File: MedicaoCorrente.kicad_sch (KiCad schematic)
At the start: 11 parts, among them J1 Conn_01x02, J2 Conn_01x02, J3 Conn_01x02, U4 LM324

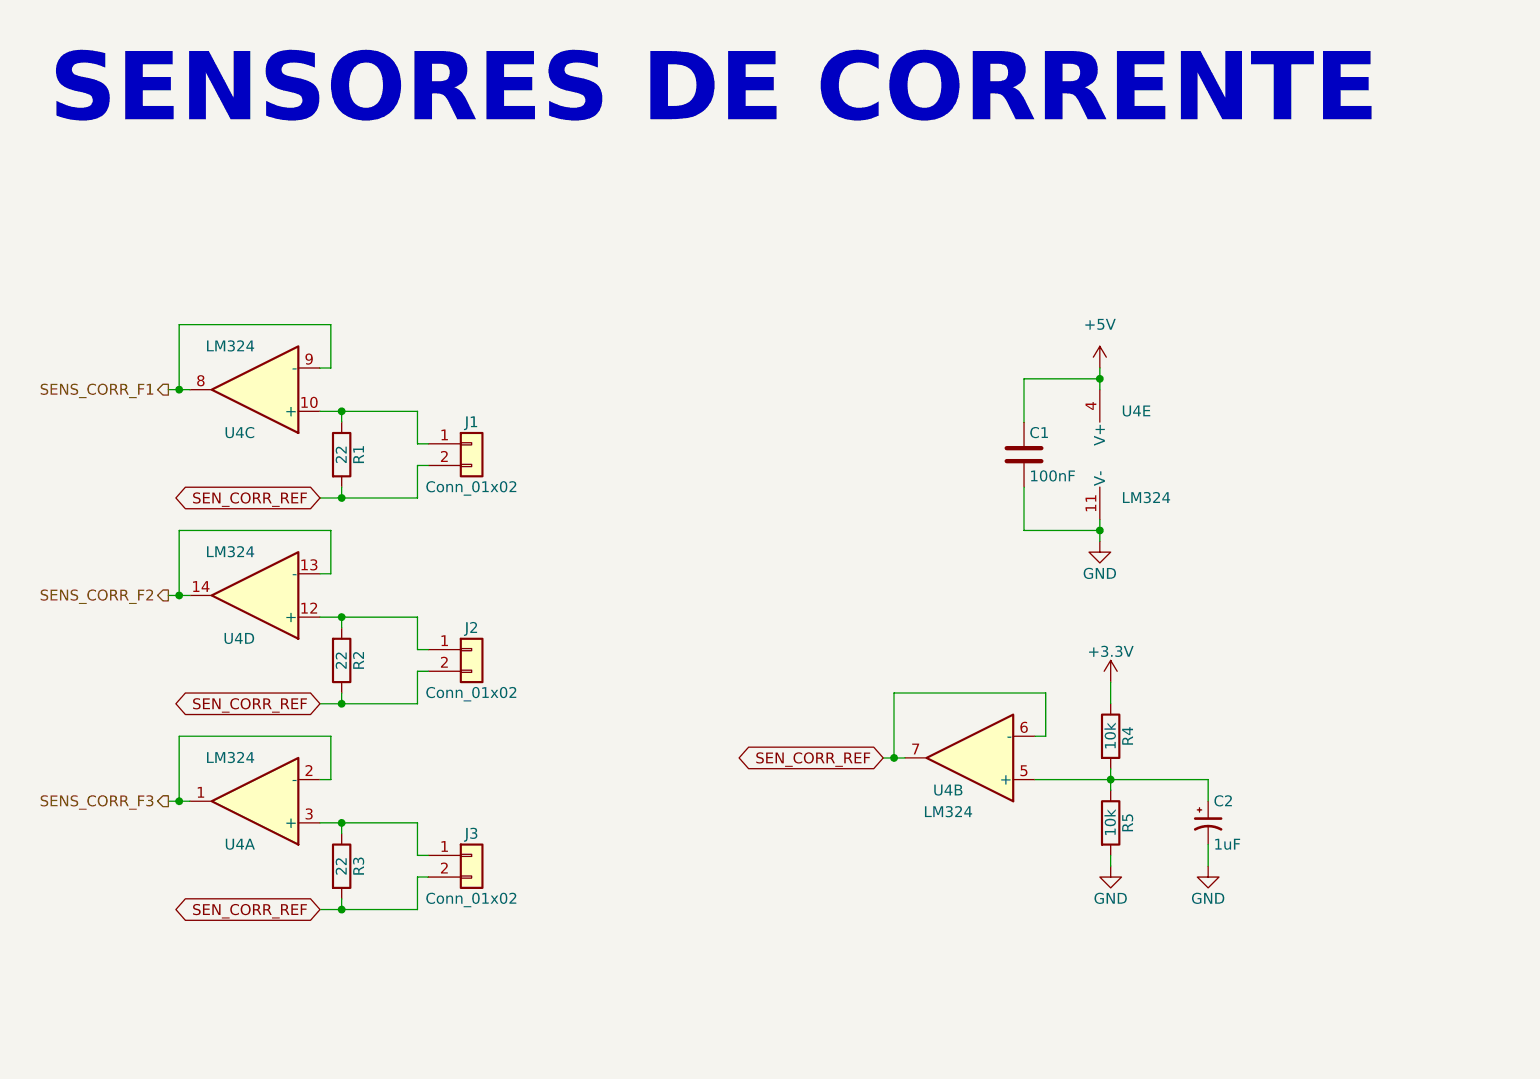
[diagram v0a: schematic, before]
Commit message: Adicionado zeners de proteção para a saída dos buffers
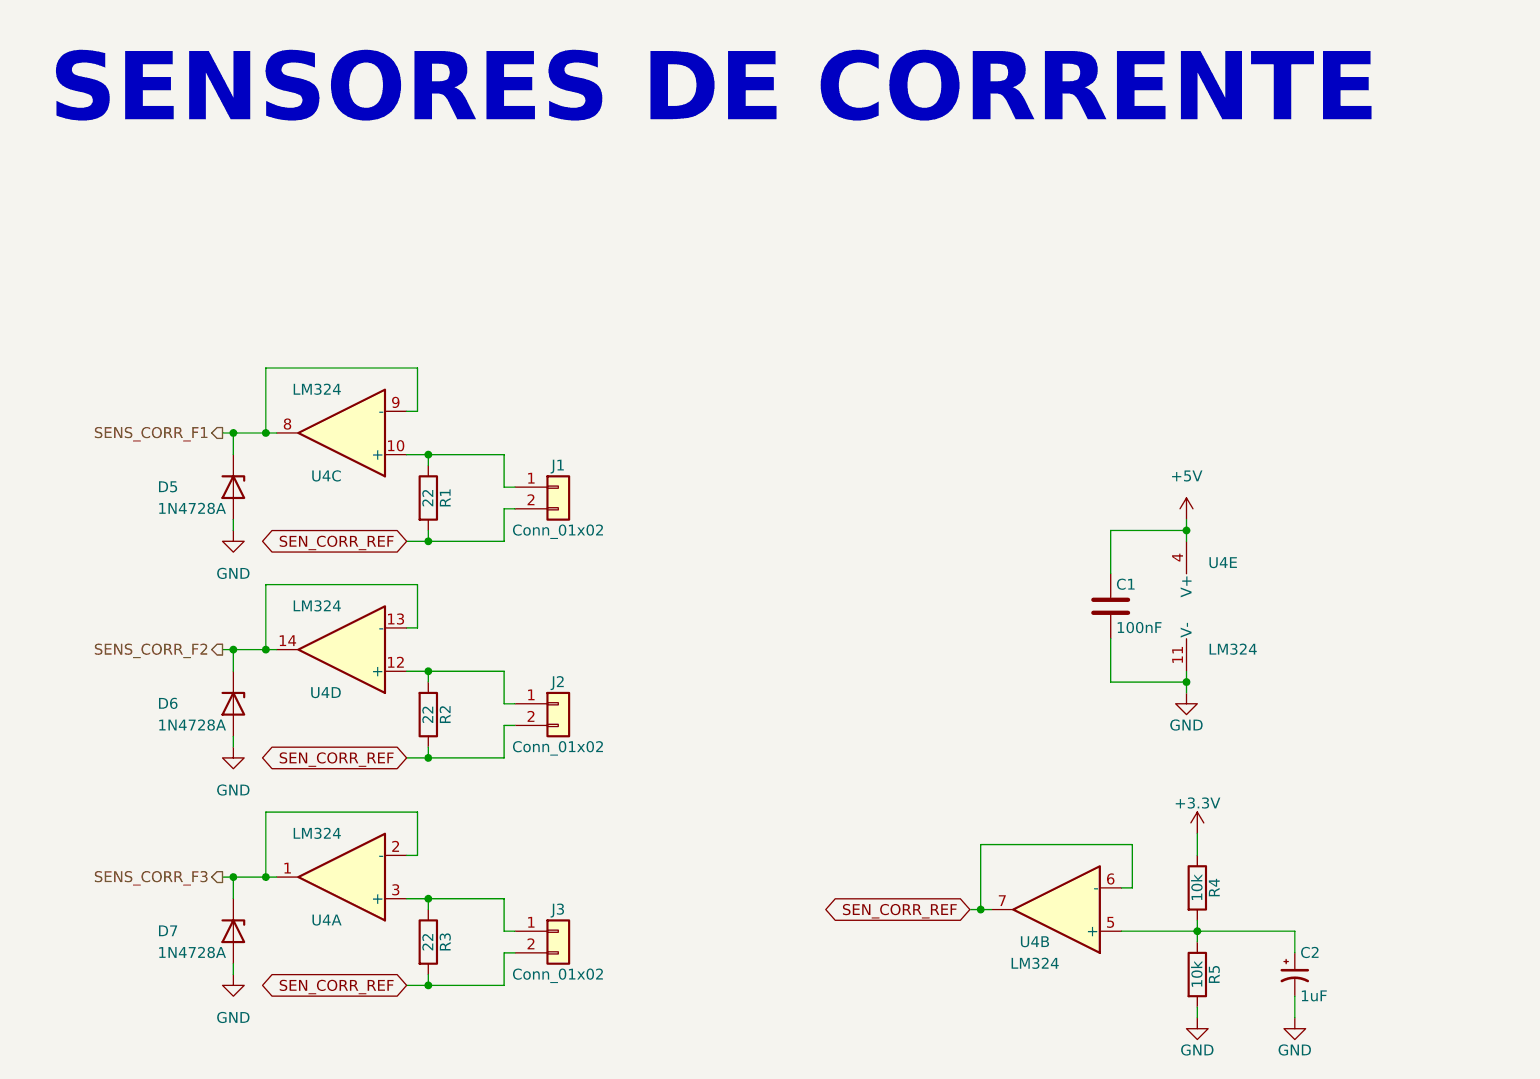
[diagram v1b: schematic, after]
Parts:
- added D5, D6, D7: 1N4728A, Diode_THT:D_DO-41_SOD81_P10.16mm_Horizontal, symbol Diode:1N47xxA
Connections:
- net GND: now also D5.2 (A), D6.2 (A), D7.2 (A)
- net SENS_CORR_F1: now also D5.1 (K)
- net SENS_CORR_F2: now also D6.1 (K)
- net SENS_CORR_F3: now also D7.1 (K)
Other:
- moved on the sheet: C1, C2, J1, J2, J3, R1, R2, R3, R4, R5, U4A, U4B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

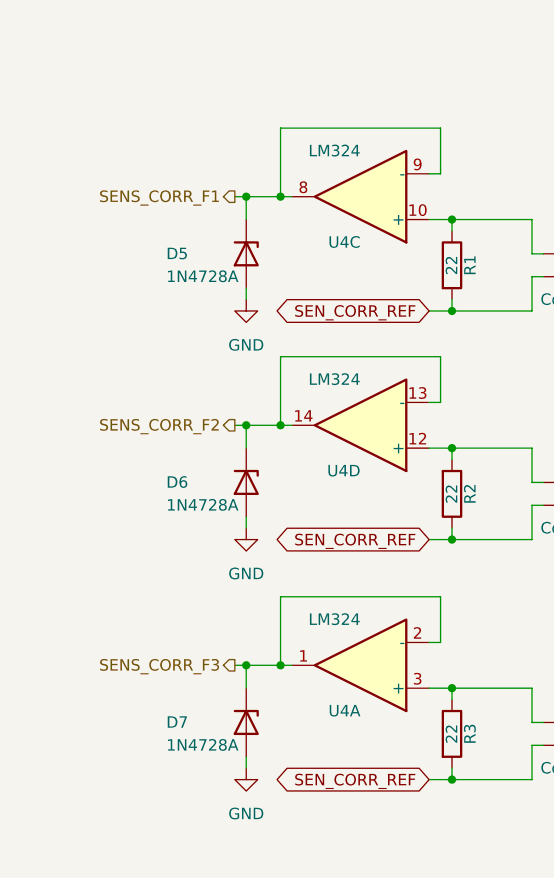
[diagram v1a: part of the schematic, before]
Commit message: As proteções nas saídas dos amplificadores operacionais foram melhoradas e os trimpots foram substituídos por trimpots de 3 pinos, para refletir os que são comprados por aqui.
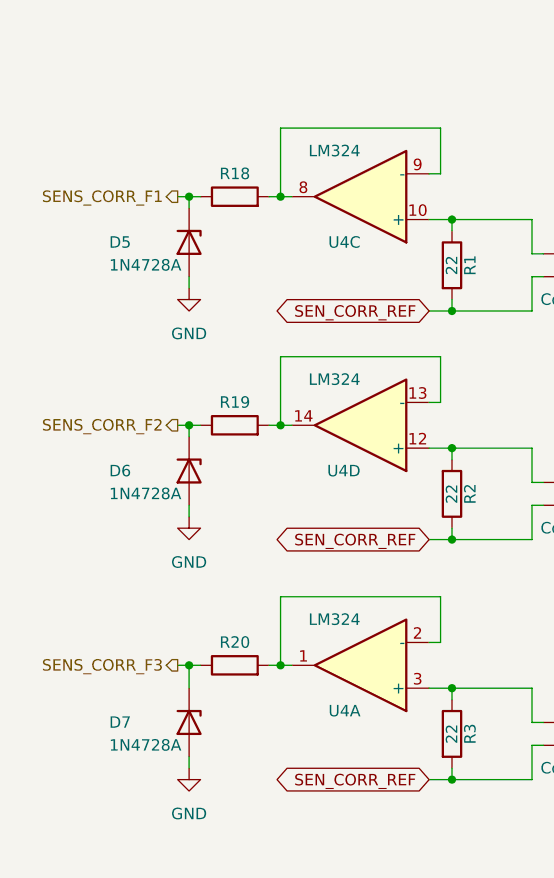
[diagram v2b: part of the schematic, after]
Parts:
- added R18, R19, R20: (no value), symbol Device:R
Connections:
- net SENS_CORR_F1: now also R18.1; no longer U4.8, U4.9 (-)
- net SENS_CORR_F2: now also R19.1; no longer U4.13 (-), U4.14
- net SENS_CORR_F3: now also R20.1; no longer U4.1, U4.2 (-)
- new net: R19.2, U4.13 (-), U4.14
- new net: R18.2, U4.8, U4.9 (-)
- new net: R20.2, U4.1, U4.2 (-)
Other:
- moved on the sheet: D5, D6, D7

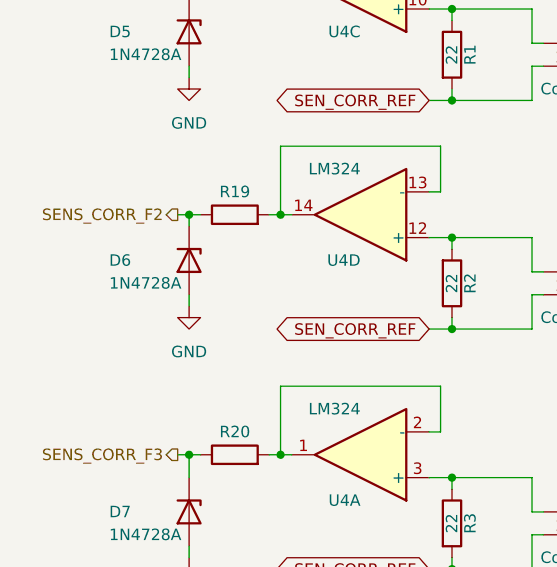
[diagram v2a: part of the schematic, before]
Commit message: Definido todos os footprints para os componentes e feito o DRC
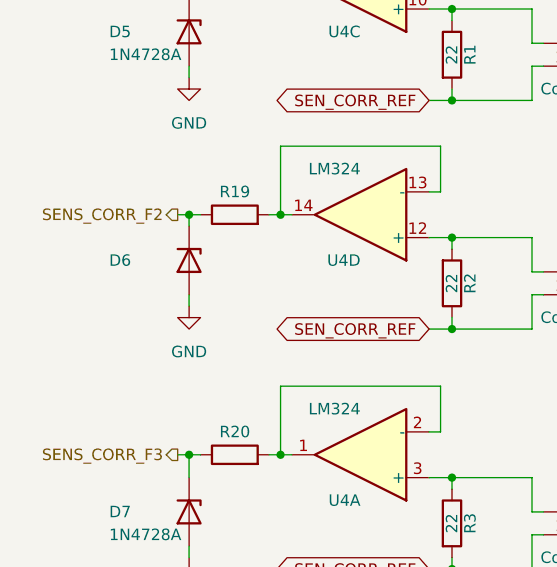
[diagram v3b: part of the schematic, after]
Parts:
- D6: value 1N4728A -> (none); footprint Diode_THT:D_DO-41_SOD81_P10.16mm_Horizontal -> (none)
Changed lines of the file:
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@@
     (pin "1")
   )
-  (symbol (lib_id "Diode:1N47xxA") (at 87.63 104.14 270) (unit 1)
+  (symbol (lib_name "1N47xxA_1") (lib_id "Diode:1N47xxA") (at 87.63 104.14 270) (unit 1)
     (in_bom yes) (on_board yes)
     (property "Reference" "D6" (id 0) (at 78.74 104.14 90)
       (effects (font (size 1.27 1.27)) (justify left))
     )
-    (property "Value" "1N4728A" (id 1) (at 78.74 106.68 90)
+    (property "Value" "" (id 1) (at 78.74 106.68 90)
       (effects (font (size 1.27 1.27)) (justify left))
     )
-    (property "Footprint" "Diode_THT:D_DO-41_SOD81_P10.16mm_Horizontal" (id 2) (at 83.185 104.14 0)
+    (property "Footprint" "" (id 2) (at 83.185 104.14 0)
       (effects (font (size 1.27 1.27)) hide)
     )

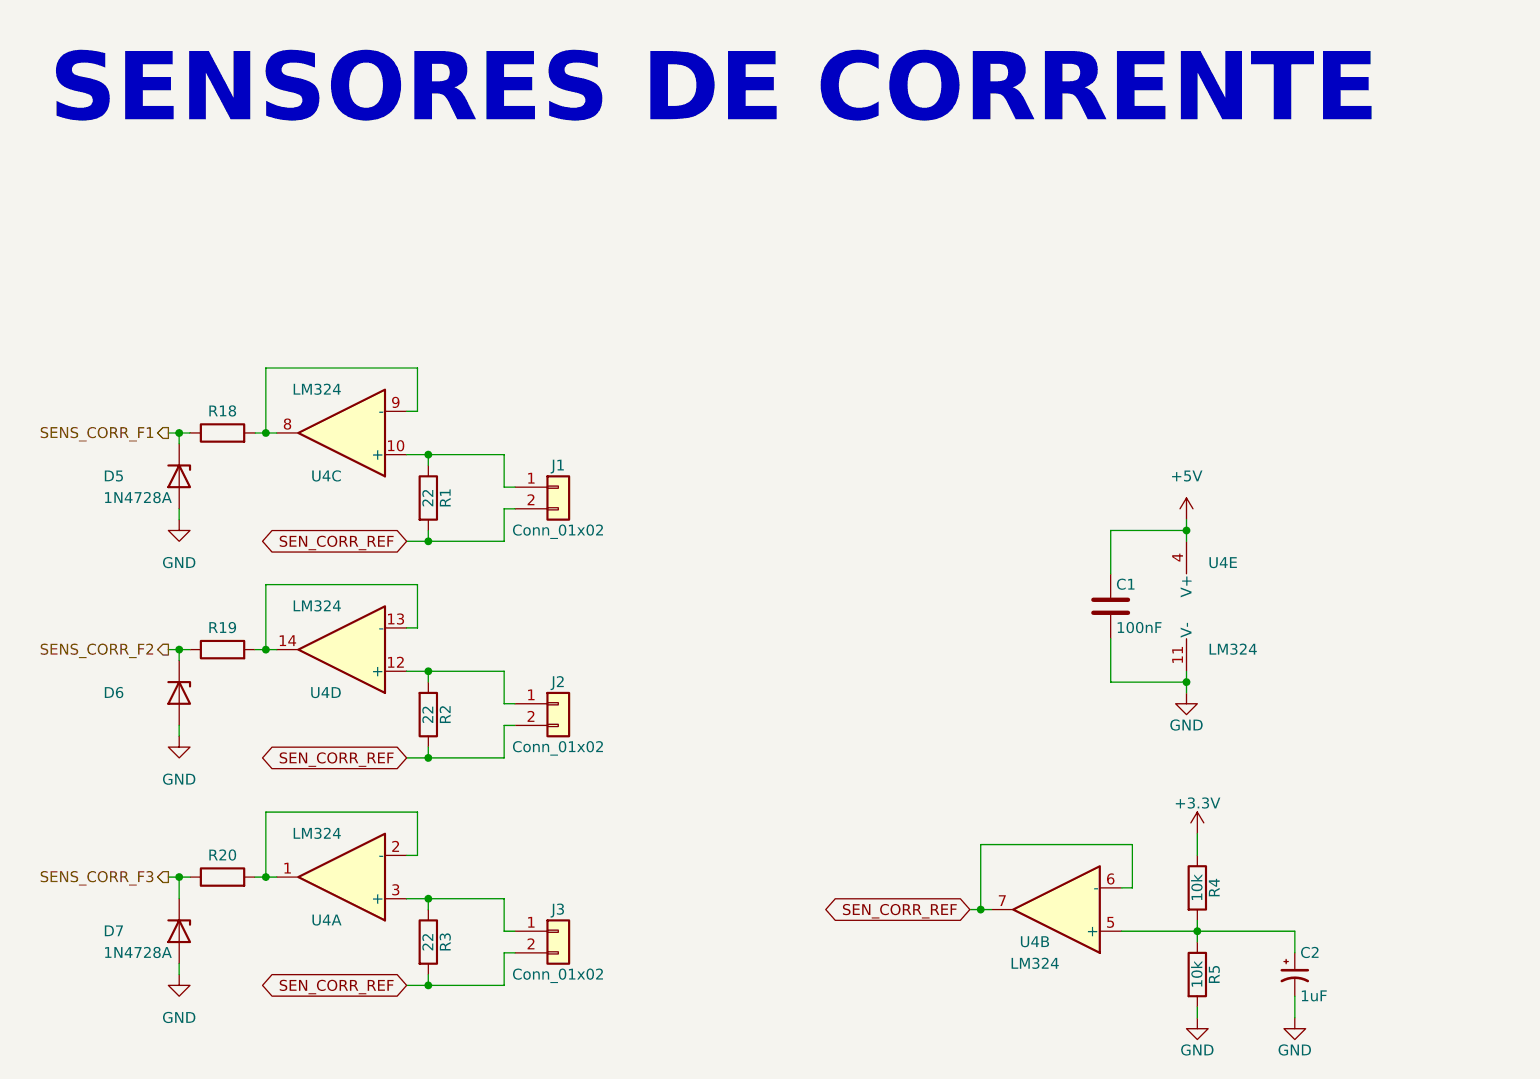
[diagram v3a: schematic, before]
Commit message: PCB e modelo 3D foram completados. As alterações necessárias foram feitas no esquemático para refletir o projeto desenvolvido na PCB. Teve-se que alterar o modelo do ESP32 para aquele que foi adquirido para o projeto.
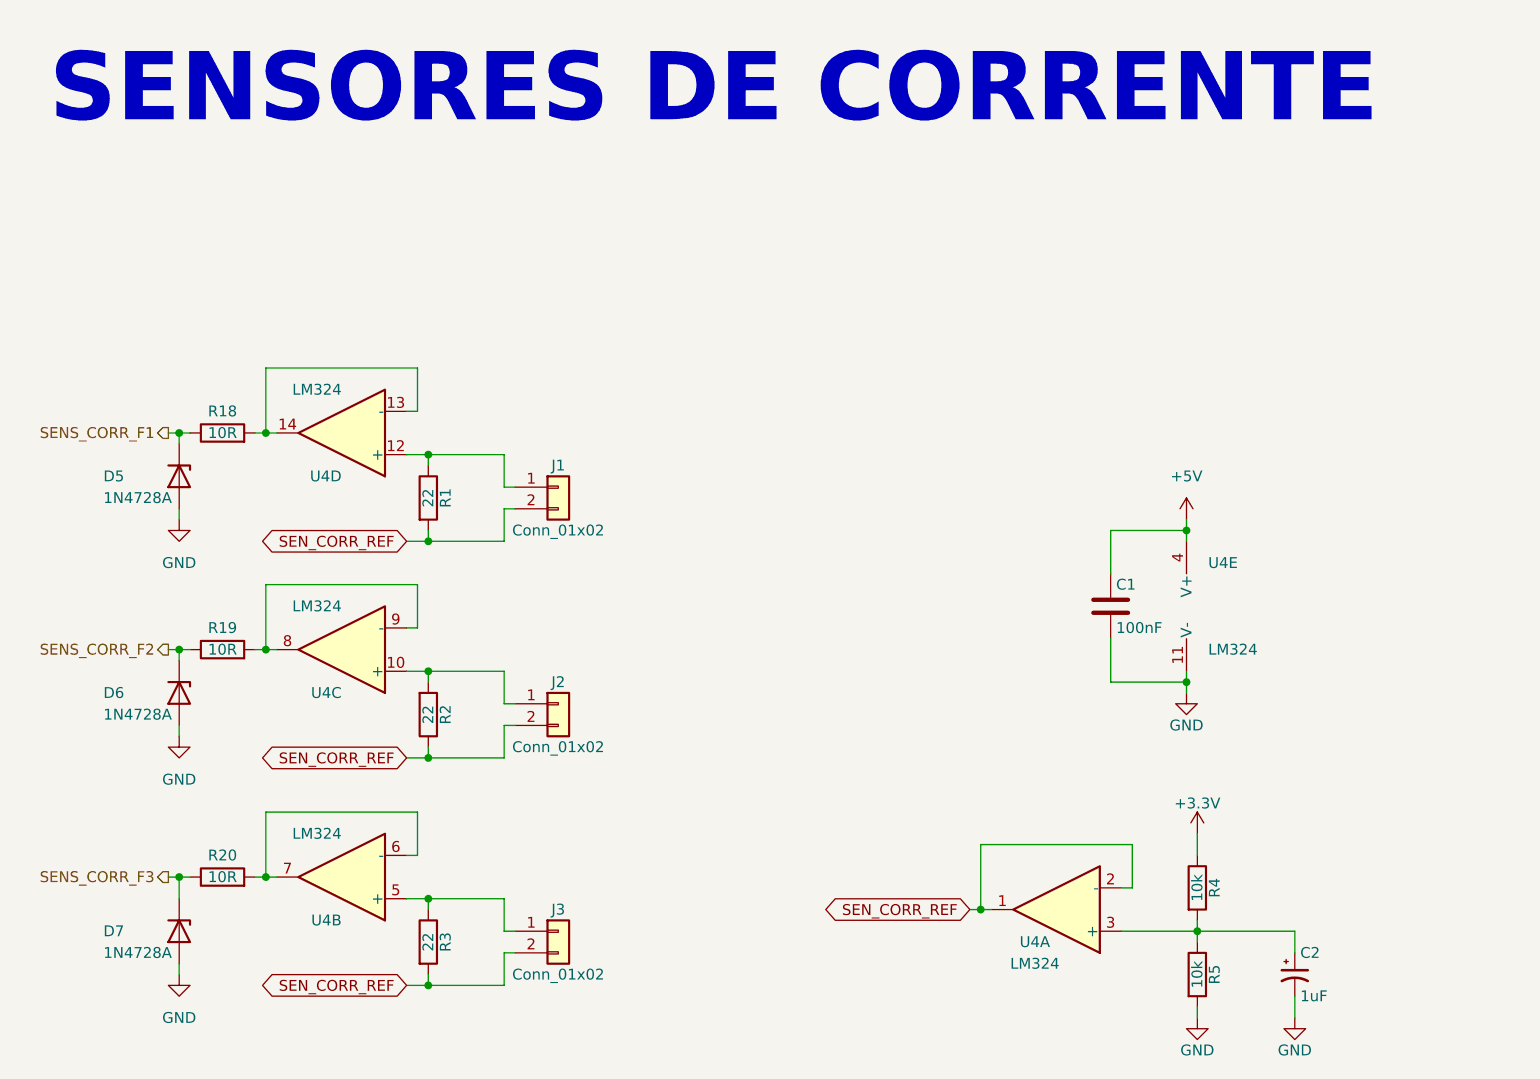
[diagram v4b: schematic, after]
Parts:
- D6: value (none) -> 1N4728A; footprint (none) -> Diode_THT:D_DO-41_SOD81_P10.16mm_Horizontal
- R18, R19, R20: value (none) -> 10R; footprint (none) -> Resistor_THT:R_Axial_DIN0207_L6.3mm_D2.5mm_P2.54mm_Vertical
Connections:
- net SEN_CORR_REF: now also U4.1, U4.2 (-); no longer U4.6 (-), U4.7
- net at C2.1, R4.2, R5.1: now also U4.3 (+); no longer U4.5 (+)
- net at J1.1 (Pin_1), R1.1: now also U4.12 (+); no longer U4.10 (+)
- net at J3.1 (Pin_1), R3.1: now also U4.5 (+); no longer U4.3 (+)
- net at J2.1 (Pin_1), R2.2: now also U4.10 (+); no longer U4.12 (+)
- new net: R19.2, U4.8, U4.9 (-)
- new net: R18.2, U4.13 (-), U4.14
- new net: R20.2, U4.6 (-), U4.7
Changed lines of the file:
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@@
     (in_bom yes) (on_board yes)
     (property "Reference" "R19" (id 0) (at 92.71 96.52 90))
-    (property "Value" "" (id 1) (at 92.71 99.06 90))
-    (property "Footprint" "" (id 2) (at 92.71 100.838 90)
+    (property "Value" "10R" (id 1) (at 92.71 99.06 90))
+    (property "Footprint" "Resistor_THT:R_Axial_DIN0207_L6.3mm_D2.5mm_P2.54mm_Vertical" (id 2) (at 92.71 100.838 90)
       (effects (font (size 1.27 1.27)) hide)
     )
@@
       (effects (font (size 1.27 1.27)) (justify left))
     )
-    (property "Value" "" (id 1) (at 78.74 106.68 90)
-      (effects (font (size 1.27 1.27)) (justify left))
-    )
-    (property "Footprint" "" (id 2) (at 83.185 104.14 0)
+    (property "Value" "1N4728A" (id 1) (at 78.74 106.68 90)
+      (effects (font (size 1.27 1.27)) (justify left))
+    )
+    (property "Footprint" "Diode_THT:D_DO-41_SOD81_P10.16mm_Horizontal" (id 2) (at 83.185 104.14 0)
       (effects (font (size 1.27 1.27)) hide)
     )
@@
     (pin "2")
   )
-  (symbol (lib_id "Amplifier_Operational:LM324") (at 106.68 73.66 180) (unit 3)
+  (symbol (lib_id "Amplifier_Operational:LM324") (at 106.68 73.66 180) (unit 4)
     (in_bom yes) (on_board yes)
     (property "Reference" "U4" (id 0) (at 106.68 78.74 0)
@@
     (pin "1")
   )
-  (symbol (lib_id "Amplifier_Operational:LM324") (at 106.68 99.06 180) (unit 4)
+  (symbol (lib_id "Amplifier_Operational:LM324") (at 106.68 99.06 180) (unit 3)
     (in_bom yes) (on_board yes)
     (property "Reference" "U4" (id 0) (at 106.68 104.14 0)
@@
     (in_bom yes) (on_board yes)
     (property "Reference" "R20" (id 0) (at 92.71 123.19 90))
-    (property "Value" "" (id 1) (at 92.71 125.73 90))
-    (property "Footprint" "" (id 2) (at 92.71 127.508 90)
+    (property "Value" "10R" (id 1) (at 92.71 125.73 90))
+    (property "Footprint" "Resistor_THT:R_Axial_DIN0207_L6.3mm_D2.5mm_P2.54mm_Vertical" (id 2) (at 92.71 127.508 90)
       (effects (font (size 1.27 1.27)) hide)
     )
@@
     (pin "2")
   )
-  (symbol (lib_id "Amplifier_Operational:LM324") (at 190.5 129.54 180) (unit 2)
+  (symbol (lib_id "Amplifier_Operational:LM324") (at 190.5 129.54 180) (unit 1)
     (in_bom yes) (on_board yes)
     (property "Reference" "U4" (id 0) (at 187.96 133.35 0))
@@
     (pin "4")
   )
-  (symbol (lib_id "Amplifier_Operational:LM324") (at 106.68 125.73 180) (unit 1)
+  (symbol (lib_id "Amplifier_Operational:LM324") (at 106.68 125.73 180) (unit 2)
     (in_bom yes) (on_board yes)
     (property "Reference" "U4" (id 0) (at 106.68 130.81 0)
@@
     (in_bom yes) (on_board yes)
     (property "Reference" "R18" (id 0) (at 92.71 71.12 90))
-    (property "Value" "" (id 1) (at 92.71 73.66 90))
-    (property "Footprint" "" (id 2) (at 92.71 75.438 90)
-      (effects (font (size 1.27 1.27)) hide)
-    )
+    (property "Value" "10R" (id 1) (at 92.71 73.66 90))
+    (property "Footprint" "Resistor_THT:R_Axial_DIN0207_L6.3mm_D2.5mm_P2.54mm_Vertical" (id 2) (at 92.71 75.438 90)
+      (effects (font (size 1.27 1.27)) hide)
+    )
